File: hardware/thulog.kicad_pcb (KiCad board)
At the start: 2 copper layers, 28.4 x 30 mm, 16 parts, among them IC1 ATTINY2313A-S, K1 DHT, P1 ISP, P2 USBmini, X1 QUARTZCMS4

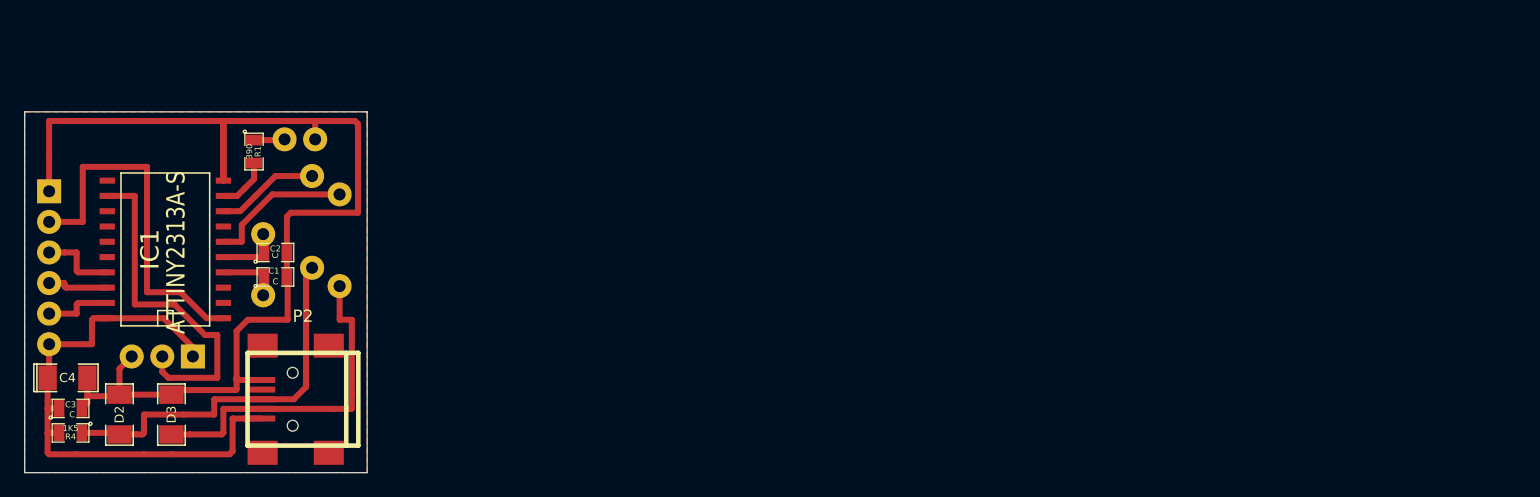
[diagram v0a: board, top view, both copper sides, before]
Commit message: updated schema and code cumatch existing pcb
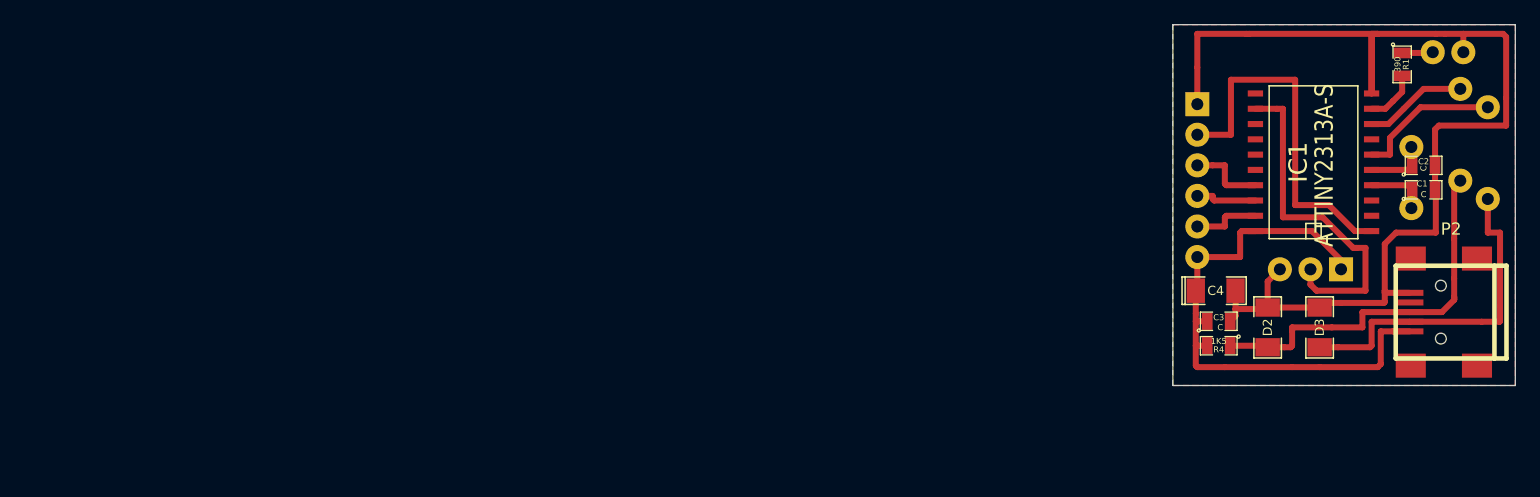
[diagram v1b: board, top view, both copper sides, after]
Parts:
- moved C3 95.7 mm to (248.0, 56.0)
- moved D1 95.7 mm to (267.1, 33.7)
- moved D2 95.7 mm to (252.1, 56.5)
- moved D3 95.7 mm to (256.4, 56.5)
- moved IC1 95.7 mm to (255.9, 42.8)
- moved K1 95.7 mm to (255.7, 51.7)
- moved R1 95.7 mm to (263.3, 34.7)
- moved R4 95.7 mm to (248.0, 58.0)
- moved X1 95.7 mm to (264.0, 44.1)
- moved C1 95.7 mm to (265.0, 45.1)
- moved C2 95.7 mm to (265.0, 43.1)
- moved C4 95.7 mm to (247.8, 53.5)
- moved P1 95.7 mm to (246.3, 44.3)
- moved P2 95.7 mm to (267.3, 55.2)
- moved R2 95.7 mm to (270.4, 42.0)
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
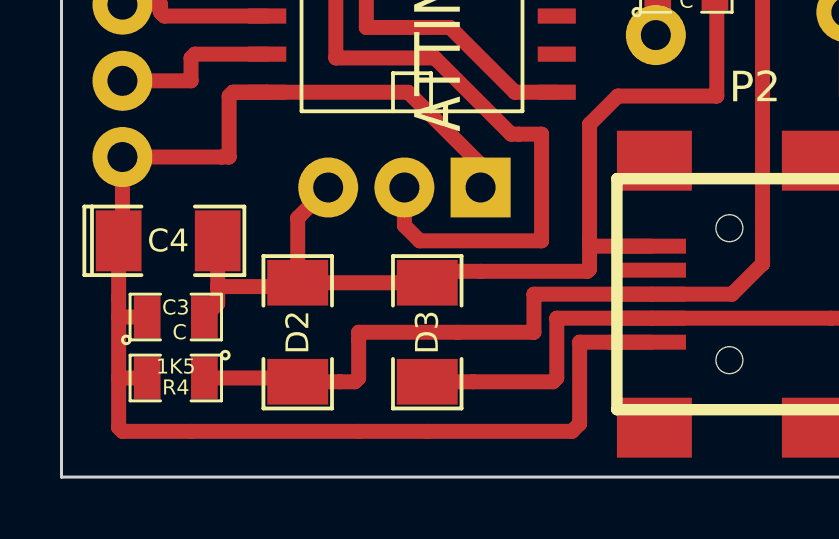
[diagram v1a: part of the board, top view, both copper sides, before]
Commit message: fixed bug in pcb d+ pullup resistor to VCC instead of d-. Now the usb is recognised
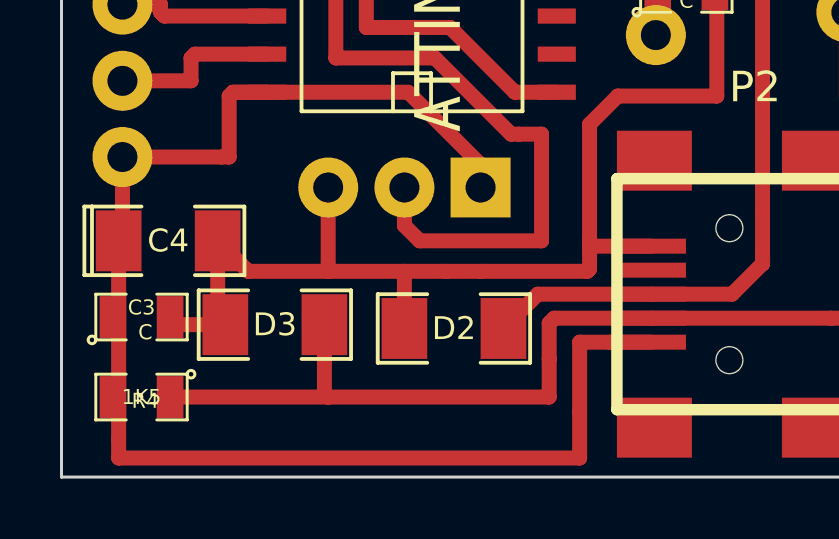
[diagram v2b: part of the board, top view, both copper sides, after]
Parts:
- moved D2 5.21 mm to (257.3, 56.4), turned to 0 degrees
- moved D3 5.09 mm to (251.3, 56.3), turned to 0 degrees
- moved R4 1.31 mm to (246.9, 58.7)
- moved C3 1.14 mm to (246.9, 56.0)
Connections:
- D3 pad 2: N-0000025 -> N-0000023
- P2 pad 2: N-0000025 -> N-0000023
- R2 pad 2: N-0000025 -> N-0000023
- R4 pad 1: N-0000024 -> N-0000023
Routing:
- net N-0000023: track 0.00 -> 39.7 mm
- net N-0000025: track 28.7 -> 0.00 mm
- net N-0000024: track 32.5 -> 20.2 mm
- net GND: track 95.9 -> 99.4 mm
